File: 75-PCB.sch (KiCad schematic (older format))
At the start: 195 parts

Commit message: Added switch for split right shift support
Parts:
- added D?: SOD-123, symbol Device:D_Small
- added MX_LSHIFT2: MX-LED, symbol MX_Alps_Hybrid:MX-LED
- renumbered MX_LSHIFT to MX_LSHIFT1, MX_LSHIFT to MX_RSHIFT
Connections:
- net COL1: now also MX_LSHIFT2.1 (COL); no longer MX_Z.1 (COL)
- net COL10: now also MX_..1 (COL); no longer MX_/.1 (COL)
- net COL11: now also MX_/.1 (COL); no longer MX_RSHIFT.1 (COL)
- net COL12: now also MX_RSHIFT.1 (COL)
- net COL2: now also MX_Z.1 (COL); no longer MX_X.1 (COL)
- net COL3: now also MX_X.1 (COL); no longer MX_C.1 (COL)
- net COL4: now also MX_C.1 (COL); no longer MX_V.1 (COL)
- net COL5: now also MX_V.1 (COL); no longer MX_B.1 (COL)
- net COL6: now also MX_B.1 (COL); no longer MX_N.1 (COL)
- net COL7: now also MX_N.1 (COL); no longer MX_M.1 (COL)
- net COL8: now also MX_M.1 (COL); no longer MX_,.1 (COL)
- net COL9: now also MX_,.1 (COL); no longer MX_..1 (COL)
- new net: D?.2 (A), MX_LSHIFT2.2 (ROW)
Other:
- moved on the sheet: D?, MX_,, MX_., MX_/, MX_B, MX_C, MX_M, MX_N, MX_RSHIFT, MX_V, MX_X, MX_Z
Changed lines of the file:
@@
 $EndComp
 $Comp
-L MX_Alps_Hybrid:MX-LED MX_LSHIFT
+L MX_Alps_Hybrid:MX-LED MX_LSHIFT1
 U 1 1 65140663
 P 1100 6700
-F 0 "MX_LSHIFT" H 1182 6924 60  0000 C CNN
+F 0 "MX_LSHIFT1" H 1182 6924 60  0000 C CNN
 F 1 "MX-LED" H 1182 6850 20  0000 C CNN
 F 2 "" H 475 6675 60  0001 C CNN
@@
 L MX_Alps_Hybrid:MX-LED MX_Z
 U 1 1 65140669
-P 1750 6700
-F 0 "MX_Z" H 1832 6924 60  0000 C CNN
-F 1 "MX-LED" H 1832 6850 20  0000 C CNN
-F 2 "" H 1125 6675 60  0001 C CNN
-F 3 "" H 1125 6675 60  0001 C CNN
-	1    1750 6700
-	1    0    0    -1
-$EndComp
-$Comp
-L MX_Alps_Hybrid:MX-LED MX_X
-U 1 1 6514066F
 P 2400 6700
-F 0 "MX_X" H 2482 6924 60  0000 C CNN
+F 0 "MX_Z" H 2482 6924 60  0000 C CNN
 F 1 "MX-LED" H 2482 6850 20  0000 C CNN
 F 2 "" H 1775 6675 60  0001 C CNN
@@
 $EndComp
 $Comp
-L MX_Alps_Hybrid:MX-LED MX_C
-U 1 1 65140675
+L MX_Alps_Hybrid:MX-LED MX_X
+U 1 1 6514066F
 P 3050 6700
-F 0 "MX_C" H 3132 6924 60  0000 C CNN
+F 0 "MX_X" H 3132 6924 60  0000 C CNN
 F 1 "MX-LED" H 3132 6850 20  0000 C CNN
 F 2 "" H 2425 6675 60  0001 C CNN
@@
 $EndComp
 $Comp
-L MX_Alps_Hybrid:MX-LED MX_V
-U 1 1 6514067B
+L MX_Alps_Hybrid:MX-LED MX_C
+U 1 1 65140675
 P 3700 6700
-F 0 "MX_V" H 3782 6924 60  0000 C CNN
+F 0 "MX_C" H 3782 6924 60  0000 C CNN
 F 1 "MX-LED" H 3782 6850 20  0000 C CNN
 F 2 "" H 3075 6675 60  0001 C CNN
@@
 $EndComp
 $Comp
-L MX_Alps_Hybrid:MX-LED MX_B
-U 1 1 65140681
+L MX_Alps_Hybrid:MX-LED MX_V
+U 1 1 6514067B
 P 4350 6700
-F 0 "MX_B" H 4432 6924 60  0000 C CNN
+F 0 "MX_V" H 4432 6924 60  0000 C CNN
 F 1 "MX-LED" H 4432 6850 20  0000 C CNN
 F 2 "" H 3725 6675 60  0001 C CNN
@@
 $EndComp
 $Comp
-L MX_Alps_Hybrid:MX-LED MX_N
-U 1 1 65140687
+L MX_Alps_Hybrid:MX-LED MX_B
+U 1 1 65140681
 P 5000 6700
-F 0 "MX_N" H 5082 6924 60  0000 C CNN
+F 0 "MX_B" H 5082 6924 60  0000 C CNN
 F 1 "MX-LED" H 5082 6850 20  0000 C CNN
 F 2 "" H 4375 6675 60  0001 C CNN
@@
 $EndComp
 $Comp
-L MX_Alps_Hybrid:MX-LED MX_M
-U 1 1 6514068D
+L MX_Alps_Hybrid:MX-LED MX_N
+U 1 1 65140687
 P 5650 6700
-F 0 "MX_M" H 5732 6924 60  0000 C CNN
+F 0 "MX_N" H 5732 6924 60  0000 C CNN
 F 1 "MX-LED" H 5732 6850 20  0000 C CNN
 F 2 "" H 5025 6675 60  0001 C CNN
 F 3 "" H 5025 6675 60  0001 C CNN
 	1    5650 6700
+	1    0    0    -1
+$EndComp
+$Comp
+L MX_Alps_Hybrid:MX-LED MX_M
+U 1 1 6514068D
+P 6300 6700
+F 0 "MX_M" H 6382 6924 60  0000 C CNN
+F 1 "MX-LED" H 6382 6850 20  0000 C CNN
+F 2 "" H 5675 6675 60  0001 C CNN
+F 3 "" H 5675 6675 60  0001 C CNN
+	1    6300 6700
 	1    0    0    -1
 $EndComp
@@
 $EndComp
 $Comp
-L MX_Alps_Hybrid:MX-LED MX_LSHIFT
+L MX_Alps_Hybrid:MX-LED MX_RSHIFT
 U 1 1 651406A5
+P 8900 6700
+F 0 "MX_RSHIFT" H 8982 6924 60  0000 C CNN
+F 1 "MX-LED" H 8982 6850 20  0000 C CNN
+F 2 "" H 8275 6675 60  0001 C CNN
+F 3 "" H 8275 6675 60  0001 C CNN
+	1    8900 6700
+	1    0    0    -1
+$EndComp
+$Comp
+L MX_Alps_Hybrid:MX-LED MX_/
+U 1 1 6514069F
 P 8250 6700
-F 0 "MX_LSHIFT" H 8332 6924 60  0000 C CNN
+F 0 "MX_/" H 8332 6924 60  0000 C CNN
 F 1 "MX-LED" H 8332 6850 20  0000 C CNN
 F 2 "" H 7625 6675 60  0001 C CNN
@@
 $EndComp
 $Comp
-L MX_Alps_Hybrid:MX-LED MX_/
-U 1 1 6514069F
+L MX_Alps_Hybrid:MX-LED MX_.
+U 1 1 65140699
 P 7600 6700
-F 0 "MX_/" H 7682 6924 60  0000 C CNN
+F 0 "MX_." H 7682 6924 60  0000 C CNN
 F 1 "MX-LED" H 7682 6850 20  0000 C CNN
 F 2 "" H 6975 6675 60  0001 C CNN
@@
 $EndComp
 $Comp
-L MX_Alps_Hybrid:MX-LED MX_.
-U 1 1 65140699
+L MX_Alps_Hybrid:MX-LED MX_,
+U 1 1 65140693
 P 6950 6700
-F 0 "MX_." H 7032 6924 60  0000 C CNN
+F 0 "MX_," H 7032 6924 60  0000 C CNN
 F 1 "MX-LED" H 7032 6850 20  0000 C CNN
 F 2 "" H 6325 6675 60  0001 C CNN
 F 3 "" H 6325 6675 60  0001 C CNN
 	1    6950 6700
-	1    0    0    -1
-$EndComp
-$Comp
-L MX_Alps_Hybrid:MX-LED MX_,
-U 1 1 65140693
-P 6300 6700
-F 0 "MX_," H 6382 6924 60  0000 C CNN
-F 1 "MX-LED" H 6382 6850 20  0000 C CNN
-F 2 "" H 5675 6675 60  0001 C CNN
-F 3 "" H 5675 6675 60  0001 C CNN
-	1    6300 6700
 	1    0    0    -1
 $EndComp
@@
 Wire Wire Line
 	1900 5750 1900 4850
-Connection ~ 1900 6650
-Wire Wire Line
-	1900 6650 1900 5750
 Connection ~ 2550 3050
 Wire Wire Line
@@
 	2550 4850 2550 5750
 Connection ~ 2550 5750
-Wire Wire Line
-	2550 5750 2550 6650
-Connection ~ 2550 6650
 Wire Wire Line
 	3200 6650 3200 5750
@@
 Wire Wire Line
 	4500 5750 4500 4850
-Connection ~ 4500 6650
-Wire Wire Line
-	4500 6650 4500 5750
 Connection ~ 5150 3050
 Wire Wire Line
@@
 Wire Wire Line
 	7100 5750 7100 4850
-Connection ~ 7100 6650
-Wire Wire Line
-	7100 6650 7100 5750
 Connection ~ 7750 3050
 Wire Wire Line
@@
 	7750 4850 7750 5750
 Connection ~ 7750 5750
-Wire Wire Line
-	7750 5750 7750 6650
-Connection ~ 7750 6650
 Wire Wire Line
 	8400 6650 8400 5750
@@
 Wire Wire Line
 	1250 6650 1250 7550
-Wire Wire Line
-	1900 6650 1900 7550
-Wire Wire Line
-	2550 6650 2550 7550
-Wire Wire Line
-	4500 6650 4500 7550
-Wire Wire Line
-	7100 6650 7100 7550
-Wire Wire Line
-	7750 6650 7750 7550
-Connection ~ 6450 6650
-Wire Wire Line
-	6450 6650 6450 7550
-Wire Wire Line
-	6450 5750 6450 6650
 Text GLabel 1250 2750 2    50   Input ~ 0
 COL0
@@
 L Device:D_Small D?
 U 1 1 5F6F79BE
-P 1600 6950
-F 0 "D?" H 1650 7150 50  0000 R CNN
-F 1 "SOD-123" H 1750 7050 50  0000 R CNN
-F 2 "" V 1600 6950 50  0001 C CNN
-F 3 "~" V 1600 6950 50  0001 C CNN
-	1    1600 6950
-	0    -1   -1   0
-$EndComp
-$Comp
-L Device:D_Small D?
-U 1 1 5F703720
 P 2250 6950
 F 0 "D?" H 2300 7150 50  0000 R CNN
@@
 $Comp
 L Device:D_Small D?
-U 1 1 5F70F572
+U 1 1 5F703720
 P 2900 6950
 F 0 "D?" H 2950 7150 50  0000 R CNN
@@
 $Comp
 L Device:D_Small D?
-U 1 1 5F71B428
+U 1 1 5F70F572
 P 3550 6950
 F 0 "D?" H 3600 7150 50  0000 R CNN
@@
 $Comp
 L Device:D_Small D?
-U 1 1 5F7273A1
+U 1 1 5F71B428
 P 4200 6950
 F 0 "D?" H 4250 7150 50  0000 R CNN
@@
 $Comp
 L Device:D_Small D?
-U 1 1 5F733284
+U 1 1 5F7273A1
 P 4850 6950
 F 0 "D?" H 4900 7150 50  0000 R CNN
@@
 $Comp
 L Device:D_Small D?
-U 1 1 5F73F2AC
+U 1 1 5F733284
 P 5500 6950
 F 0 "D?" H 5550 7150 50  0000 R CNN
@@
 $Comp
 L Device:D_Small D?
-U 1 1 5F74B329
+U 1 1 5F73F2AC
 P 6150 6950
 F 0 "D?" H 6200 7150 50  0000 R CNN
@@
 $Comp
 L Device:D_Small D?
-U 1 1 5F7571A8
+U 1 1 5F74B329
 P 6800 6950
 F 0 "D?" H 6850 7150 50  0000 R CNN
@@
 $Comp
 L Device:D_Small D?
-U 1 1 5F762F4B
+U 1 1 5F7571A8
 P 7450 6950
 F 0 "D?" H 7500 7150 50  0000 R CNN
@@
 $Comp
 L Device:D_Small D?
-U 1 1 5F76EDD4
+U 1 1 5F762F4B
 P 8100 6950
 F 0 "D?" H 8150 7150 50  0000 R CNN
@@
 F 3 "~" V 8100 6950 50  0001 C CNN
 	1    8100 6950
+	0    -1   -1   0
+$EndComp
+$Comp
+L Device:D_Small D?
+U 1 1 5F76EDD4
+P 8750 6950
+F 0 "D?" H 8800 7150 50  0000 R CNN
+F 1 "SOD-123" H 8900 7050 50  0000 R CNN
+F 2 "" V 8750 6950 50  0001 C CNN
+F 3 "~" V 8750 6950 50  0001 C CNN
+	1    8750 6950
 	0    -1   -1   0
 $EndComp
@@
 Wire Wire Line
 	11200 7050 10700 7050
-Connection ~ 1600 7050
-Wire Wire Line
-	1600 7050 950  7050
-Connection ~ 2250 7050
-Wire Wire Line
-	2250 7050 1600 7050
-Connection ~ 2900 7050
-Wire Wire Line
-	2900 7050 2250 7050
-Connection ~ 3550 7050
-Wire Wire Line
-	3550 7050 2900 7050
-Connection ~ 4200 7050
-Wire Wire Line
-	4200 7050 3550 7050
-Connection ~ 4850 7050
-Wire Wire Line
-	4850 7050 4200 7050
-Connection ~ 5500 7050
-Wire Wire Line
-	5500 7050 4850 7050
-Connection ~ 6150 7050
-Wire Wire Line
-	6150 7050 5500 7050
-Connection ~ 6800 7050
-Wire Wire Line
-	6800 7050 6150 7050
-Connection ~ 7450 7050
-Wire Wire Line
-	7450 7050 6800 7050
-Connection ~ 8100 7050
-Wire Wire Line
-	8100 7050 7450 7050
 Connection ~ 10050 7050
-Wire Wire Line
-	10050 7050 8100 7050
 Connection ~ 10700 7050
 Wire Wire Line
@@
 	950  6850 1050 6850
 Wire Wire Line
-	1600 6850 1700 6850
-Wire Wire Line
 	2250 6850 2350 6850
 Wire Wire Line
@@
 Wire Wire Line
 	8100 6850 8200 6850
+Wire Wire Line
+	8750 6850 8850 6850
 Wire Wire Line
 	10050 6850 10150 6850
@@
 Wire Wire Line
 	10700 3250 10800 3250
+Connection ~ 8750 7050
+Wire Wire Line
+	8750 7050 10050 7050
+Wire Wire Line
+	9050 5750 9050 6650
+Connection ~ 9050 5750
+Connection ~ 8100 7050
+Wire Wire Line
+	8100 7050 8750 7050
+Wire Wire Line
+	7750 5750 7750 6650
+Connection ~ 7450 7050
+Wire Wire Line
+	7450 7050 8100 7050
+Connection ~ 7750 6650
+Wire Wire Line
+	7750 6650 7750 7550
+Wire Wire Line
+	7100 5750 7100 6650
+Connection ~ 6800 7050
+Wire Wire Line
+	6800 7050 7450 7050
+Connection ~ 7100 6650
+Wire Wire Line
+	7100 6650 7100 7550
+Wire Wire Line
+	6450 5750 6450 6650
+Connection ~ 6150 7050
+Wire Wire Line
+	6150 7050 6800 7050
+Connection ~ 6450 6650
+Wire Wire Line
+	6450 6650 6450 7550
+Connection ~ 5500 7050
+Wire Wire Line
+	5500 7050 6150 7050
+Connection ~ 4850 7050
+Wire Wire Line
+	4850 7050 5500 7050
+Wire Wire Line
+	4500 5750 4500 6650
+Connection ~ 4200 7050
+Wire Wire Line
+	4200 7050 4850 7050
+Connection ~ 4500 6650
+Wire Wire Line
+	4500 6650 4500 7550
+Connection ~ 3550 7050
+Wire Wire Line
+	3550 7050 4200 7050
+Connection ~ 2900 7050
+Wire Wire Line
+	2900 7050 3550 7050
+Wire Wire Line
+	2550 5750 2550 6650
+Connection ~ 2250 7050
+Wire Wire Line
+	2250 7050 2900 7050
+Connection ~ 2550 6650
+Wire Wire Line
+	2550 6650 2550 7550
+Wire Wire Line
+	1900 5750 1900 6650
+Wire Wire Line
+	950  7050 2250 7050
+$Comp
+L MX_Alps_Hybrid:MX-LED MX_LSHIFT2
+U 1 1 5EAD32D7
+P 1750 6700
+F 0 "MX_LSHIFT2" H 1832 6924 60  0000 C CNN
+F 1 "MX-LED" H 1832 6850 20  0000 C CNN
+F 2 "" H 1125 6675 60  0001 C CNN
+F 3 "" H 1125 6675 60  0001 C CNN
+	1    1750 6700
+	1    0    0    -1
+$EndComp
+$Comp
+L Device:D_Small D?
+U 1 1 5EAD32DD
+P 1600 6950
+F 0 "D?" H 1650 7150 50  0000 R CNN
+F 1 "SOD-123" H 1750 7050 50  0000 R CNN
+F 2 "" V 1600 6950 50  0001 C CNN
+F 3 "~" V 1600 6950 50  0001 C CNN
+	1    1600 6950
+	0    -1   -1   0
+$EndComp
+Wire Wire Line
+	1600 6850 1700 6850
+Connection ~ 1900 6650
+Wire Wire Line
+	1900 6650 1900 7550
 $EndSCHEMATC

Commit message: Added switches for multiple layouts
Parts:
- added D: SOD-123, symbol Device:D_Small
- added MX_ENTER2, MX_LALT, MX_LCTRL?, MX_LSHIFT2, MX_RALT?, MX_RCTRL?, MX_SPACE2, MX_SPACE3, MX_SPACE4, MX_SPACE5, MX_\2: MX-LED, symbol MX_Alps_Hybrid:MX-LED
- USB1: renamed from USB?; footprint (none) -> Type-C:Wurth-632723300011-HandSoldering
- gave numbers to parts that had none: 27
- renumbered MX_' to MX_'1, MX_, to MX_,1, MX_- to MX_-1, MX_. to MX_.1, MX_/ to MX_/1, MX_; to MX_;1, MX_= to MX_=1, MX_A to MX_A1, MX_B to MX_B1, MX_C to MX_C1, MX_CAPS to MX_CAPS1, MX_D to MX_D1, MX_DEL to MX_DEL1, MX_DOWN to MX_DOWN1, MX_E to MX_E1, MX_END to MX_END1, MX_ENTER to MX_ENTER1, MX_ESC to MX_ESC1, MX_F to MX_F1, MX_G to MX_G1, MX_H to MX_H1, MX_HOME to MX_HOME1, MX_I to MX_I1, MX_J to MX_J1, MX_K to MX_K1, MX_L to MX_L1, MX_LALT to MX_LALT1, MX_LCTRL to MX_LCTRL1, MX_LEFT to MX_LEFT1, MX_LSHIFT2 to MX_LSHIFT3, MX_LWIN to MX_LWIN1, MX_M to MX_M1, MX_N to MX_N1, MX_O to MX_O1, MX_P to MX_P1, MX_PAUSE to MX_PAUSE1, MX_PGDN to MX_PGDN1, MX_PGUP to MX_PGUP1, MX_Q to MX_Q1, MX_R to MX_R1, MX_RALT to MX_RALT1, MX_RCTRL to MX_RCTRL1, MX_RIGHT to MX_RIGHT1, MX_RSHIFT to MX_RSHIFT1, MX_RWIN to MX_RWIN1, MX_S to MX_S1, MX_SPACE to MX_SPACE1, MX_T to MX_T1, MX_TAB to MX_TAB1, MX_U to MX_U1, MX_UP to MX_UP1, MX_V to MX_V1, MX_W to MX_W1, MX_X to MX_X1, MX_Y to MX_Y1, MX_Z to MX_Z1, MX_[ to MX_[1, MX_\ to MX_\1, MX_] to MX_]1, MX_` to MX_`1
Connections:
- net COL0: now also MX_LCTRL?.1 (COL), MX_LSHIFT2.1 (COL)
- net COL10: now also MX_RALT?.1 (COL)
- net COL12: now also MX_ENTER2.1 (COL)
- net COL13: now also MX_\2.1 (COL)
- net COL2: now also MX_LALT.1 (COL)
- net COL4: now also MX_SPACE4.1 (COL)
- net COL5: now also MX_SPACE2.1 (COL), MX_SPACE3.1 (COL)
- net COL8: now also MX_RCTRL?.1 (COL)
- net GND: now also USB1.26 (Connector_Legs)
- net ROW5: now also D.1 (K)
- net at D.2 (A), MX_\1.2 (ROW): now also MX_\2.2 (ROW)
- net at D.2 (A), MX_ENTER1.2 (ROW): now also MX_ENTER2.2 (ROW)
- net at D.2 (A), MX_LSHIFT1.2 (ROW): now also MX_LSHIFT2.2 (ROW)
- net at D.2 (A), MX_B1.2 (ROW): now also MX_SPACE5.2 (ROW)
- net at D.2 (A), MX_RCTRL1.2 (ROW): now also MX_RALT?.2 (ROW)
- net at D.2 (A), MX_RALT1.2 (ROW): now also MX_RCTRL?.2 (ROW)
- net at D.2 (A), MX_SPACE1.2 (ROW): now also MX_SPACE2.2 (ROW), MX_SPACE3.2 (ROW)
- net at D.2 (A), MX_LALT1.2 (ROW): now also MX_LALT.2 (ROW)
- net at D.2 (A), MX_LCTRL1.2 (ROW): now also MX_LCTRL?.2 (ROW)
- new net: D.2 (A), MX_SPACE4.2 (ROW)

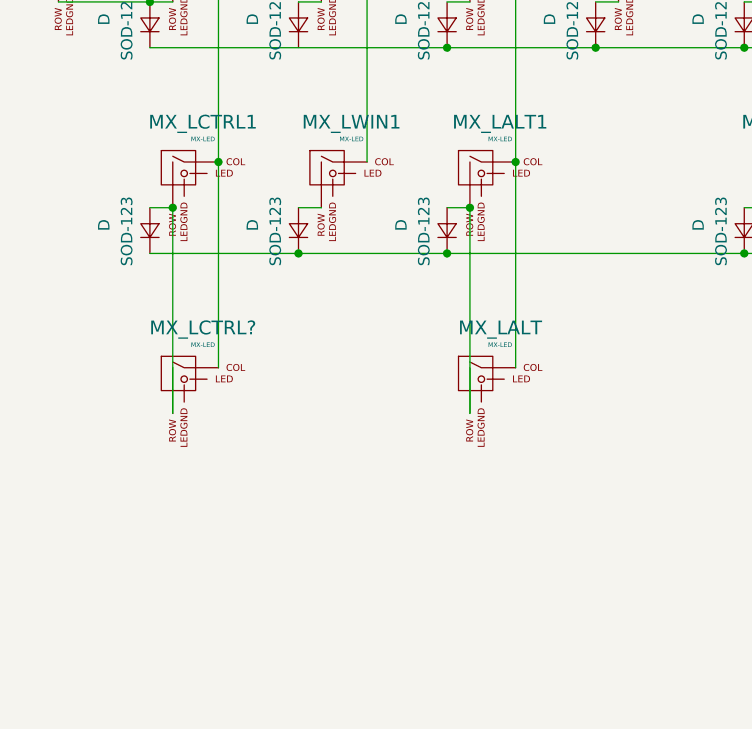
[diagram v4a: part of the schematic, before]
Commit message: Added switches for modifiers for 7U spacebar
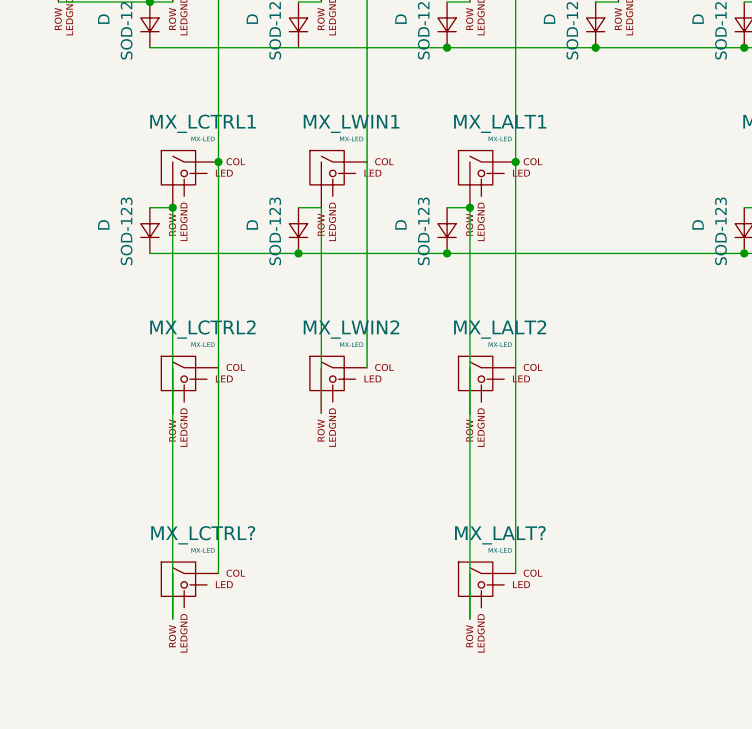
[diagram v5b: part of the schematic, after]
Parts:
- added MX_LALT?, MX_LCTRL?, MX_LWIN2: MX-LED, symbol MX_Alps_Hybrid:MX-LED
- gave numbers to parts that had none: 1
- renumbered MX_LALT to MX_LALT2
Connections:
- net COL0: now also MX_LCTRL?.1 (COL)
- net COL1: now also MX_LWIN2.1 (COL)
- net COL2: now also MX_LALT?.1 (COL)
- net at D.2 (A), MX_LCTRL1.2 (ROW), MX_LCTRL2.2 (ROW): now also MX_LCTRL?.2 (ROW)
- net at D.2 (A), MX_LALT1.2 (ROW), MX_LALT2.2 (ROW): now also MX_LALT?.2 (ROW)
- net at D.2 (A), MX_LWIN1.2 (ROW): now also MX_LWIN2.2 (ROW)
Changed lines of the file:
@@
 	3550 7950 2250 7950
 $Comp
-L MX_Alps_Hybrid:MX-LED MX_LCTRL?
+L MX_Alps_Hybrid:MX-LED MX_LCTRL2
 U 1 1 5EB2F6D3
 P 1100 8500
-F 0 "MX_LCTRL?" H 1182 8724 60  0000 C CNN
+F 0 "MX_LCTRL2" H 1182 8724 60  0000 C CNN
 F 1 "MX-LED" H 1182 8650 20  0000 C CNN
 F 2 "" H 475 8475 60  0001 C CNN
@@
 $EndComp
 $Comp
-L MX_Alps_Hybrid:MX-LED MX_LALT
+L MX_Alps_Hybrid:MX-LED MX_LALT2
 U 1 1 5EB62996
 P 2400 8500
-F 0 "MX_LALT" H 2482 8724 60  0000 C CNN
+F 0 "MX_LALT2" H 2482 8724 60  0000 C CNN
 F 1 "MX-LED" H 2482 8650 20  0000 C CNN
 F 2 "" H 1775 8475 60  0001 C CNN
@@
 	550  6850 950  6850
 Connection ~ 950  6850
+$Comp
+L MX_Alps_Hybrid:MX-LED MX_LCTRL?
+U 1 1 5F0D2C14
+P 1100 9400
+F 0 "MX_LCTRL?" H 1182 9624 60  0000 C CNN
+F 1 "MX-LED" H 1182 9550 20  0000 C CNN
+F 2 "" H 475 9375 60  0001 C CNN
+F 3 "" H 475 9375 60  0001 C CNN
+	1    1100 9400
+	1    0    0    -1
+$EndComp
+$Comp
+L MX_Alps_Hybrid:MX-LED MX_LALT?
+U 1 1 5F0D2C1A
+P 2400 9400
+F 0 "MX_LALT?" H 2482 9624 60  0000 C CNN
+F 1 "MX-LED" H 2482 9550 20  0000 C CNN
+F 2 "" H 1775 9375 60  0001 C CNN
+F 3 "" H 1775 9375 60  0001 C CNN
+	1    2400 9400
+	1    0    0    -1
+$EndComp
+Wire Wire Line
+	2350 9550 2350 8650
+Wire Wire Line
+	2550 9350 2550 8450
+Wire Wire Line
+	1250 9350 1250 8450
+Wire Wire Line
+	1050 9550 1050 8650
+$Comp
+L MX_Alps_Hybrid:MX-LED MX_LWIN2
+U 1 1 5F107680
+P 1750 8500
+F 0 "MX_LWIN2" H 1832 8724 60  0000 C CNN
+F 1 "MX-LED" H 1832 8650 20  0000 C CNN
+F 2 "" H 1125 8475 60  0001 C CNN
+F 3 "" H 1125 8475 60  0001 C CNN
+	1    1750 8500
+	1    0    0    -1
+$EndComp
+Wire Wire Line
+	1700 8650 1700 7750
+Wire Wire Line
+	1900 8450 1900 7550
 $EndSCHEMATC

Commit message: Finished LED backlight matrix
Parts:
- added D?: SOD-123, symbol Device:D_Small
- added Q?: 2N7002, Package_TO_SOT_SMD:SOT-23, symbol Transistor_FET:2N7002
- added R10, R? (x87): 1K, symbol Device:R_Small
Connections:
- net +5V: now also MX_#1.3 (LED), MX_#10.3 (LED), MX_#2.3 (LED), MX_#3.3 (LED), MX_#4.3 (LED), MX_#5.3 (LED), MX_#6.3 (LED), MX_#7.3 (LED), MX_#8.3 (LED), MX_#9.3 (LED), MX_'1.3 (LED), MX_,1.3 (LED), MX_-1.3 (LED), MX_.1.3 (LED), MX_/1.3 (LED), MX_;1.3 (LED), MX_=1.3 (LED), MX_A1.3 (LED), MX_B1.3 (LED), MX_BCKSP1.3 (LED), MX_BCKSP2.3 (LED), MX_C1.3 (LED), MX_CAPS1.3 (LED), MX_D1.3 (LED), MX_DEL1.3 (LED), MX_DOWN1.3 (LED), MX_E1.3 (LED), MX_END1.3 (LED), MX_ENTER1.3 (LED), MX_ENTER2.3 (LED), MX_ESC1.3 (LED), MX_F#1.3 (LED), MX_F#10.3 (LED), MX_F#11.3 (LED), MX_F#12.3 (LED), MX_F#2.3 (LED), MX_F#3.3 (LED), MX_F#4.3 (LED), MX_F#5.3 (LED), MX_F#6.3 (LED), MX_F#7.3 (LED), MX_F#8.3 (LED), MX_F#9.3 (LED), MX_F1.3 (LED), MX_G1.3 (LED), MX_H1.3 (LED), MX_HOME1.3 (LED), MX_I1.3 (LED), MX_J1.3 (LED), MX_K1.3 (LED), MX_L1.3 (LED), MX_LALT1.3 (LED), MX_LALT2.3 (LED), MX_LALT?.3 (LED), MX_LCTRL1.3 (LED), MX_LCTRL2.3 (LED), MX_LCTRL?.3 (LED), MX_LEFT1.3 (LED), MX_LSHIFT1.3 (LED), MX_LSHIFT2.3 (LED), MX_LSHIFT3.3 (LED), MX_LWIN1.3 (LED), MX_LWIN2.3 (LED), MX_M1.3 (LED), MX_N1.3 (LED), MX_O1.3 (LED), MX_P1.3 (LED), MX_PAUSE1.3 (LED), MX_PGDN1.3 (LED), MX_PGUP1.3 (LED), MX_Q1.3 (LED), MX_R1.3 (LED), MX_RALT1.3 (LED), MX_RALT?.3 (LED), MX_RCTRL1.3 (LED), MX_RCTRL?.3 (LED), MX_RIGHT1.3 (LED), MX_RSHIFT1.3 (LED), MX_RWIN1.3 (LED), MX_S1.3 (LED), MX_SPACE1.3 (LED), MX_SPACE2.3 (LED), MX_SPACE3.3 (LED), MX_SPACE4.3 (LED), MX_SPACE5.3 (LED), MX_T1.3 (LED), MX_TAB1.3 (LED), MX_U1.3 (LED), MX_UP1.3 (LED), MX_V1.3 (LED), MX_W1.3 (LED), MX_X1.3 (LED), MX_Y1.3 (LED), MX_Z1.3 (LED), MX_[1.3 (LED), MX_\1.3 (LED), MX_\2.3 (LED), MX_]1.3 (LED), MX_`1.3 (LED)
- net GND: now also Q?.2 (S)
- net ROW4: now also D.1 (K)
- net ROW5: now also D?.1 (K)
- net at MX_\2.4 (LEDGND): now also MX_\1.4 (LEDGND), R?.1
- net at MX_ENTER2.4 (LEDGND): now also MX_ENTER1.4 (LEDGND), R?.1
- net at MX_SPACE2.4 (LEDGND): now also MX_SPACE1.4 (LEDGND), MX_SPACE3.4 (LEDGND), R?.1
- net at MX_SPACE4.4 (LEDGND): now also R?.1
- net at MX_LSHIFT3.4 (LEDGND): now also R?.1
- net at MX_LCTRL2.4 (LEDGND): now also MX_LCTRL1.4 (LEDGND), MX_LCTRL?.4 (LEDGND), R?.1
- net at MX_LALT2.4 (LEDGND): now also MX_LALT1.4 (LEDGND), MX_LALT?.4 (LEDGND), R?.1
- net at MX_RCTRL?.4 (LEDGND): now also MX_RALT1.4 (LEDGND), R?.1
- net at MX_RALT?.4 (LEDGND): now also MX_RCTRL1.4 (LEDGND), R?.1
- net at D.2 (A), MX_B1.2 (ROW): no longer MX_SPACE5.2 (ROW)
- net at MX_SPACE5.4 (LEDGND): now also R?.1
- net at MX_LSHIFT2.4 (LEDGND): now also MX_LSHIFT1.4 (LEDGND), R?.1
- net at MX_LWIN2.4 (LEDGND): now also MX_LWIN1.4 (LEDGND), R?.1
- net at MX_BCKSP2.4 (LEDGND): now also R?.1
- net at MX_ESC1.4 (LEDGND): now also R?.1
- net at MX_F#1.4 (LEDGND): now also R?.1
- net at MX_F#2.4 (LEDGND): now also R?.1
- net at MX_F#3.4 (LEDGND): now also R?.1
- net at MX_F#4.4 (LEDGND): now also R?.1
- net at MX_F#5.4 (LEDGND): now also R?.1
- net at MX_F#6.4 (LEDGND): now also R?.1
- net at MX_F#7.4 (LEDGND): now also R?.1
- net at MX_F#8.4 (LEDGND): now also R?.1
- net at MX_F#9.4 (LEDGND): now also R?.1
- net at MX_F#10.4 (LEDGND): now also R?.1
- net at MX_F#11.4 (LEDGND): now also R?.1
- net at MX_F#12.4 (LEDGND): now also R?.1
- net at MX_PAUSE1.4 (LEDGND): now also R?.1
- net at MX_DEL1.4 (LEDGND): now also R?.1
- net at MX_`1.4 (LEDGND): now also R?.1
- net at MX_#1.4 (LEDGND): now also R?.1
- net at MX_#2.4 (LEDGND): now also R?.1
- net at MX_#3.4 (LEDGND): now also R?.1
- net at MX_#4.4 (LEDGND): now also R?.1
- net at MX_#5.4 (LEDGND): now also R?.1
- net at MX_#6.4 (LEDGND): now also R?.1
- net at MX_#7.4 (LEDGND): now also R?.1
- net at MX_#8.4 (LEDGND): now also R?.1
- net at MX_#9.4 (LEDGND): now also R?.1
- net at MX_#10.4 (LEDGND): now also R?.1
- net at MX_-1.4 (LEDGND): now also R?.1
- net at MX_=1.4 (LEDGND): now also R?.1
- net at MX_BCKSP1.4 (LEDGND): now also R?.1
- net at MX_HOME1.4 (LEDGND): now also R?.1
- net at MX_TAB1.4 (LEDGND): now also R?.1
- net at MX_Q1.4 (LEDGND): now also R?.1
- net at MX_W1.4 (LEDGND): now also R?.1
- net at MX_E1.4 (LEDGND): now also R?.1
- net at MX_R1.4 (LEDGND): now also R?.1
- net at MX_T1.4 (LEDGND): now also R?.1
- net at MX_Y1.4 (LEDGND): now also R?.1
- net at MX_U1.4 (LEDGND): now also R?.1
- net at MX_I1.4 (LEDGND): now also R?.1
- net at MX_O1.4 (LEDGND): now also R?.1
- net at MX_P1.4 (LEDGND): now also R?.1
- net at MX_[1.4 (LEDGND): now also R?.1
- net at MX_]1.4 (LEDGND): now also R?.1
- net at MX_PGUP1.4 (LEDGND): now also R?.1
- net at MX_CAPS1.4 (LEDGND): now also R?.1
- net at MX_A1.4 (LEDGND): now also R?.1
- net at MX_S1.4 (LEDGND): now also R?.1
- net at MX_D1.4 (LEDGND): now also R?.1
- net at MX_F1.4 (LEDGND): now also R?.1
- net at MX_G1.4 (LEDGND): now also R?.1
- net at MX_H1.4 (LEDGND): now also R?.1
- net at MX_J1.4 (LEDGND): now also R?.1
- net at MX_K1.4 (LEDGND): now also R?.1
- net at MX_L1.4 (LEDGND): now also R?.1
- net at MX_;1.4 (LEDGND): now also R?.1
- net at MX_'1.4 (LEDGND): now also R?.1
- net at MX_PGDN1.4 (LEDGND): now also R?.1
- net at MX_Z1.4 (LEDGND): now also R?.1
- net at MX_X1.4 (LEDGND): now also R?.1
- net at MX_C1.4 (LEDGND): now also R?.1
- net at MX_V1.4 (LEDGND): now also R?.1
- net at MX_B1.4 (LEDGND): now also R?.1
- net at MX_N1.4 (LEDGND): now also R?.1
- net at MX_M1.4 (LEDGND): now also R?.1
- net at MX_,1.4 (LEDGND): now also R?.1
- net at MX_.1.4 (LEDGND): now also R?.1
- net at MX_/1.4 (LEDGND): now also R?.1
- net at MX_RSHIFT1.4 (LEDGND): now also R?.1
- net at MX_UP1.4 (LEDGND): now also R?.1
- net at MX_END1.4 (LEDGND): now also R?.1
- net at MX_RWIN1.4 (LEDGND): now also R?.1
- net at MX_LEFT1.4 (LEDGND): now also R?.1
- net at MX_DOWN1.4 (LEDGND): now also R?.1
- net at MX_RIGHT1.4 (LEDGND): now also R?.1
- new net: D?.2 (A), MX_SPACE5.2 (ROW)
- new net: Q?.1 (G), R10.1
- new net LEDGND: Q?.3 (D), R?.2, R?.2, R?.2, R?.2, R?.2, R?.2, R?.2, R?.2, R?.2, R?.2, R?.2, R?.2, R?.2, R?.2, R?.2, R?.2, R?.2, R?.2, R?.2, R?.2, R?.2, R?.2, R?.2, R?.2, R?.2, R?.2, R?.2, R?.2, R?.2, R?.2, R?.2, R?.2, R?.2, R?.2, R?.2, R?.2, R?.2, R?.2, R?.2, R?.2, R?.2, R?.2, R?.2, R?.2, R?.2, R?.2, R?.2, R?.2, R?.2, R?.2, R?.2, R?.2, R?.2, R?.2, R?.2, R?.2, R?.2, R?.2, R?.2, R?.2, R?.2, R?.2, R?.2, R?.2, R?.2, R?.2, R?.2, R?.2, R?.2, R?.2, R?.2, R?.2, R?.2, R?.2, R?.2, R?.2, R?.2, R?.2, R?.2, R?.2, R?.2, R?.2, R?.2, R?.2, R?.2, R?.2, R?.2
- new net LEDMOS: R10.2
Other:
- note added: "LED MOSFET\n"
- note removed: "Breakaway tabs\n"
- moved on the sheet: C1, C2, C3, C4, C5, C6, C7, D, D1, F1, J1, MX_#1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

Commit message: Added submodule for RGB LEDs
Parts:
- added R11: 10K, symbol Device:R_Small
- R10: value 1K -> 100
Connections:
- net GND: now also R11.2
- net at Q?.1 (G), R10.1: now also R11.1
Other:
- moved on the sheet: D, D?, MX_#1, MX_#10, MX_#2, MX_#3, MX_#4, MX_#5, MX_#6, MX_#7, MX_#8, MX_#9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
